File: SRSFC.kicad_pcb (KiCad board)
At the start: 2 copper layers, 6.5 x 0.7 mm, 46 parts, among them J1 SWD_interface, X1 25MHz

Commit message: added BMP388
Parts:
- added CARD1: ~, SD_CARD_READER:TF-SMD_TF-PUSH, F.Cu at (166.5, 99.1)
- moved H4 40.4 mm to (167.9, 112.8)
- moved USB1 34.9 mm to (114.3, 98.7)
- moved X1 28.9 mm to (128.9, 97.9)
- moved SW1 20.1 mm to (148.2, 100.6)
- moved U4 12.5 mm to (147.8, 105.4)
- moved H3 4.83 mm to (120.4, 112.8)
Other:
- board size 6.5 x 0.7 mm -> 1.2 x 9.2 mm

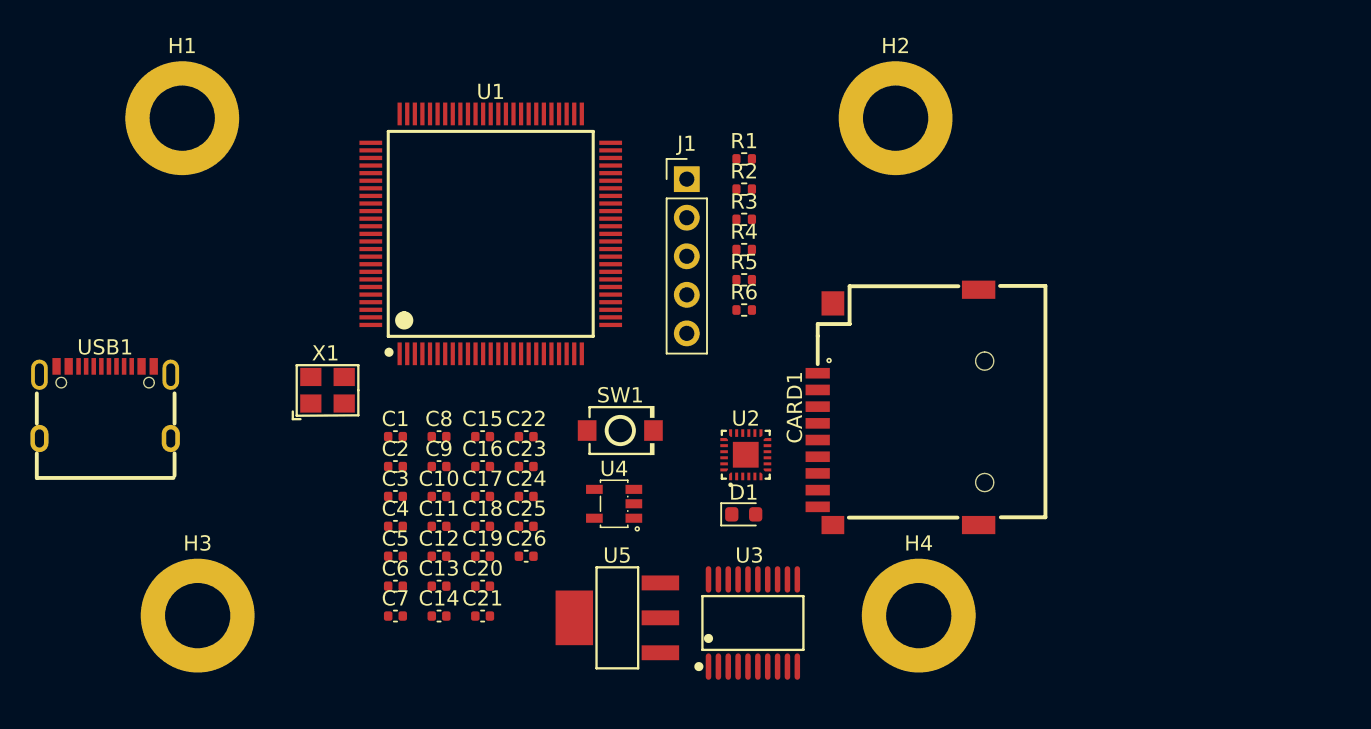
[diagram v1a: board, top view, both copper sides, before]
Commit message: added servo connectors, schema done (probably)
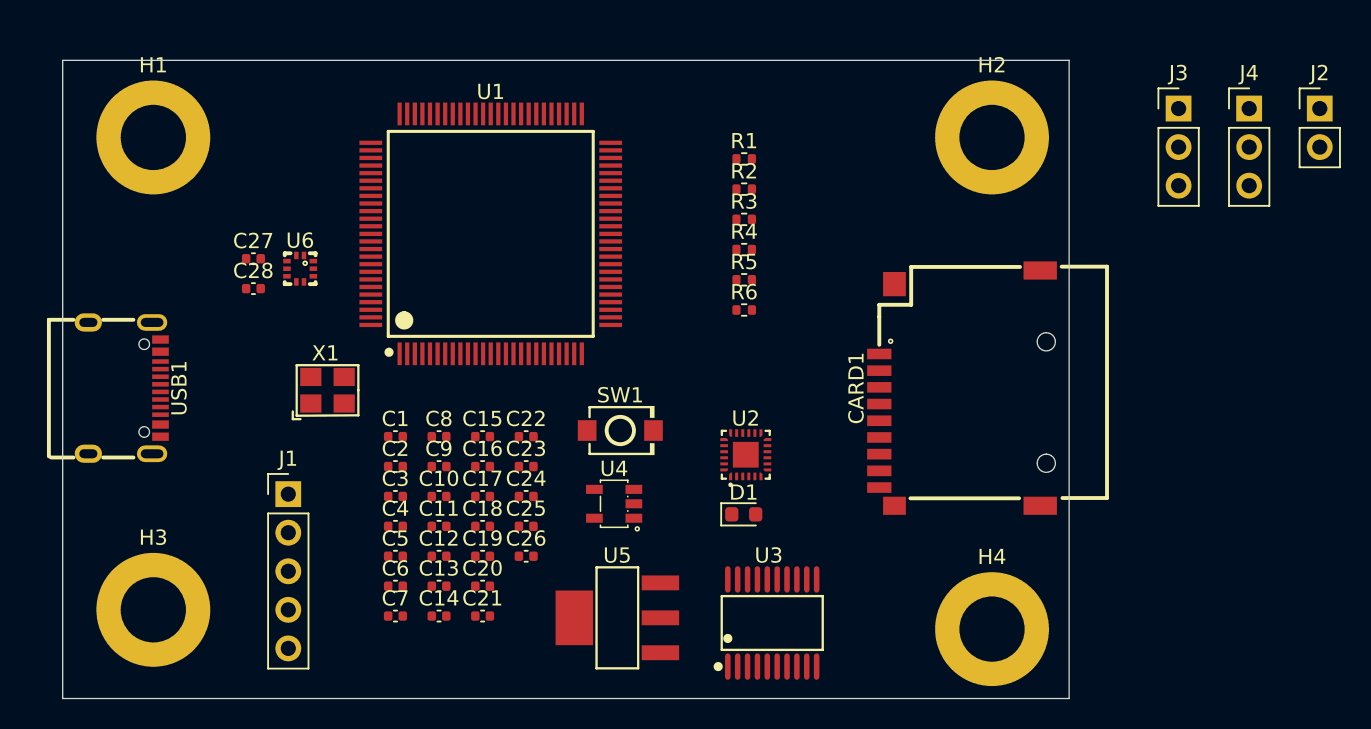
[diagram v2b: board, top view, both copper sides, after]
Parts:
- added C27: .1uF, Capacitor_SMD:C_0402_1005Metric, F.Cu at (124.1, 89.3)
- added C28: 100nF, Capacitor_SMD:C_0402_1005Metric, F.Cu at (124.1, 91.2)
- added J2: POWER, Connector_PinHeader_2.54mm:PinHeader_1x02_P2.54mm_Vertical, F.Cu at (194.3, 79.4)
- added J3: SERVO1, Connector_PinHeader_2.54mm:PinHeader_1x03_P2.54mm_Vertical, F.Cu at (185.0, 79.4)
- added J4: SERVO2, Connector_PinHeader_2.54mm:PinHeader_1x03_P2.54mm_Vertical, F.Cu at (189.7, 79.4)
- added U6: ~, BMP388:SENSORM-SMD_BMP388, F.Cu at (127.1, 89.9)
- moved J1 33.5 mm to (126.4, 104.8)
- moved H2 6.48 mm to (172.7, 81.3)
- moved H4 4.91 mm to (172.7, 113.7)
- moved CARD1 4.25 mm to (170.6, 97.8)
- moved H3 2.95 mm to (117.5, 112.4)
- moved H1 2.29 mm to (117.5, 81.3)
- moved USB1 1.58 mm to (115.6, 97.8), turned to -90 degrees
- moved U3 1.27 mm to (158.2, 113.3)
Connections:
- net +5V renamed VCC
- CARD1 pad 2: unconnected-(CARD1-CD/DAT3-Pad2) -> /SDIO_D2
- CARD1 pad 3: unconnected-(CARD1-CMD-Pad3) -> /SDIO_D3
- CARD1 pad 4: unconnected-(CARD1-VDD-Pad4) -> +3.3V
- CARD1 pad 5: unconnected-(CARD1-CLX-Pad5) -> /SDIO_SCK
- CARD1 pad 6: unconnected-(CARD1-VSS-Pad6) -> /SDIO_CMD
- CARD1 pad 7: unconnected-(CARD1-DAT0-Pad7) -> /SDIO_D0
- CARD1 pad 8: unconnected-(CARD1-DAT1-Pad8) -> /SDIO_D1
- CARD1 pad CD: unconnected-(CARD1-PadCD) -> GND
- U1 pad 65: unconnected-(U1-PC8-Pad65) -> /SDIO_D0
- U1 pad 66: unconnected-(U1-PC9-Pad66) -> /SDIO_D1
- U1 pad 67: unconnected-(U1-PA8-Pad67) -> /servo_2
- U1 pad 78: unconnected-(U1-PC10-Pad78) -> /SDIO_D2
- U1 pad 79: unconnected-(U1-PC11-Pad79) -> /SDIO_D3
- U1 pad 80: unconnected-(U1-PC12-Pad80) -> /SDIO_SCK
- U1 pad 83: unconnected-(U1-PD2-Pad83) -> /SDIO_CMD
- U1 pad 92: unconnected-(U1-PB6-Pad92) -> /servo_1
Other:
- board size 1.2 x 9.2 mm -> 66.3 x 42 mm
- copper layers 2 -> 4

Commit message: finished v1 (bad) layout)
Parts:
- C27: value .1uF -> 100nF
- R2: value 1k -> 220
- moved J2 57.7 mm to (147.3, 112.8), turned to 90 degrees
- moved J3 57.3 mm to (138.4, 112.8), turned to 90 degrees
- moved J4 53.6 mm to (144.8, 108.7), turned to 90 degrees
- moved D1 47.0 mm to (113.3, 87.4), turned to 90 degrees
- moved R2 41.4 mm to (115.1, 87.4), turned to -90 degrees
- moved R3 40.1 mm to (119.9, 103.4)
- moved R1 39.7 mm to (125.7, 108.0), turned to 90 degrees
- moved R4 38.2 mm to (119.9, 100.1)
- moved U5 37.7 mm to (116.3, 92.5)
- moved R5 35.7 mm to (126.5, 110.2), turned to 180 degrees
- moved R6 32.7 mm to (128.8, 110.2)
- moved C27 32.2 mm to (154.4, 100.1), turned to 90 degrees
- moved C25 28.6 mm to (119.9, 88.8)
- moved C24 28.1 mm to (119.9, 87.6)
- moved SW1 25.8 mm to (123.4, 107.7), turned to 90 degrees
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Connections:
- U1 pad 93: unconnected-(U1-PB7-Pad93) -> /bmp_sda
- U1 pad 95: unconnected-(U1-PB8-Pad95) -> /bmp_scl
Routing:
- net VCC: track 0.00 -> 67.2 mm
- net GND: track 0.00 -> 60.5 mm, vias 0 -> 30
- net +3.3V: track 0.00 -> 59.5 mm, vias 0 -> 16
- net /SDIO_D0: track 0.00 -> 35.8 mm, vias 0 -> 2
- net /boot0: track 0.00 -> 35.2 mm, vias 0 -> 1
- net /SDIO_D1: track 0.00 -> 35.0 mm
- net /SDIO_CMD: track 0.00 -> 35.0 mm, vias 0 -> 2
- net /SDIO_D2: track 0.00 -> 32.7 mm, vias 0 -> 2
- net /SDIO_SCK: track 0.00 -> 31.9 mm, vias 0 -> 2
- net /SDIO_D3: track 0.00 -> 31.4 mm, vias 0 -> 2
- net +1V8: track 0.00 -> 29.6 mm, vias 0 -> 3
- net /SWCLK: track 0.00 -> 27.1 mm, vias 0 -> 3
- net /USB+: track 0.00 -> 23.5 mm, vias 0 -> 2
- net /servo_1: track 0.00 -> 23.5 mm, vias 0 -> 1
- net /USB-: track 0.00 -> 22.8 mm, vias 0 -> 2
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- added copper zone on In1.Cu, net +3.3V
- added copper zone on In2.Cu, net GND
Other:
- board size 66.3 x 42 mm -> 59.9 x 37.7 mm

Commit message: good layout done, DRC passes
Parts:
- moved USB1 44.4 mm to (157.0, 85.4), turned to 180 degrees
- moved R4 36.5 mm to (155.2, 90.7), turned to -90 degrees
- moved R3 36.3 mm to (153.9, 90.7), turned to -90 degrees
- moved U5 32.2 mm to (148.1, 87.1), turned to -90 degrees
- moved C25 31.5 mm to (151.1, 92.5), turned to -90 degrees
- moved C24 30.4 mm to (149.9, 92.5), turned to -90 degrees
- moved D1 27.3 mm to (140.5, 84.3)
- moved C23 27.2 mm to (148.6, 92.5)
- moved R2 27.1 mm to (142.0, 84.3)
- moved C22 25.9 mm to (147.3, 92.5), turned to -90 degrees
- moved C1 14.2 mm to (139.4, 89.2), turned to 180 degrees
- moved C26 10.2 mm to (141.3, 110.2)
- moved J4 10.2 mm to (155.0, 109.0)
- moved J1 10.2 mm to (134.6, 112.8)
- moved J2 10.2 mm to (157.5, 112.8)
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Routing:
- net /USB-: track 22.8 -> 41.5 mm
- net /USB+: track 23.5 -> 38.9 mm
- net /SWCLK: track 27.1 -> 15.6 mm, vias 3 -> 4
- net /boot0: track 35.2 -> 46.5 mm
- net /servo_2: track 20.3 -> 30.1 mm
- net /servo_1: track 23.5 -> 32.0 mm
- net VCC: track 67.2 -> 59.3 mm
- net /SWDIO: track 17.2 -> 21.1 mm
- net Net-(USB1-CC1): track 1.47 -> 5.12 mm
- net Net-(USB1-CC2): track 1.37 -> 2.91 mm
- net GND: track 60.5 -> 61.6 mm, vias 30 -> 29
- net /nrst: track 8.76 -> 9.93 mm, vias 2 -> 0
- net +3.3V: track 59.5 -> 58.4 mm, vias 16 -> 18
- net /SDIO_CMD: track 35.0 -> 34.1 mm
- net /SDIO_D0: track 35.8 -> 35.2 mm
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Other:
- board size 59.9 x 37.7 mm -> 52.6 x 33.8 mm

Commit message: updated readme
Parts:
- removed C17, C18, C20: 100nF, Capacitor_SMD:C_0402_1005Metric
- removed C19, C21: 1uF, Capacitor_SMD:C_0402_1005Metric
- removed U3: ~, TXS0108EPWR:TSSOP-20_L6.5-W4.4-P0.65-LS6.4-BL
- removed U4: ~, LP5907MFX-1.8:SOT-23-5_L3.0-W1.7-P0.95-LS2.8-BR
- added J5: SERVO3, Connector_PinHeader_2.54mm:PinHeader_1x03_P2.54mm_Vertical, F.Cu at (147.1, 104.9)
- added J6: SERVO4, Connector_PinHeader_2.54mm:PinHeader_1x03_P2.54mm_Vertical, F.Cu at (147.1, 101.1)
- added J7: SERVO5, Connector_PinHeader_2.54mm:PinHeader_1x03_P2.54mm_Vertical, F.Cu at (147.1, 97.3)
- added JP1: address_select, Jumper:SolderJumper-2_P1.3mm_Open_RoundedPad1.0x1.5mm, B.Cu at (147.2, 109.5)
- added JP2: address_select, Jumper:SolderJumper-2_P1.3mm_Open_RoundedPad1.0x1.5mm, B.Cu at (150.7, 109.5)
- added R10: 4.7k, Resistor_SMD:R_0402_1005Metric, F.Cu at (143.5, 90.4)
- added R7: 10k, Resistor_SMD:R_0402_1005Metric, F.Cu at (143.8, 97.5)
- added R8: 10k, Resistor_SMD:R_0402_1005Metric, F.Cu at (143.8, 109.5)
- added R9: 4.7k, Resistor_SMD:R_0402_1005Metric, F.Cu at (143.5, 89.2)
- C15: value 1uF -> 100nF
- U2: footprint ICM-20948:QFN-24_L3.0-W3.0-P0.40-BL-EP -> LSM6DSOWTR:LGA-14L_L3.0-W2.5-P0.50-TL
- moved C16 11.7 mm to (143.8, 103.9), turned to 180 degrees
- moved C15 10.3 mm to (143.7, 98.8), turned to 180 degrees
- moved U2 7.72 mm to (143.8, 101.3), turned to 90 degrees
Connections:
- C15 pad 2: +1V8 -> +3.3V
- C16 pad 1: GND -> +3.3V
- C16 pad 2: +1V8 -> GND
- U1 pad 63: unconnected-(U1-PC6-Pad63) -> /servo_3
- U1 pad 64: unconnected-(U1-PC7-Pad64) -> /servo_4
- U1 pad 68: unconnected-(U1-PA9-Pad68) -> /servo_5
- U1 pad 77: /SPI_CS -> unconnected-(U1-PA15-Pad77)
- U1 pad 88: /SPI_MOSI -> unconnected-(U1-PD7-Pad88)
- U1 pad 89: /SPI_SCK -> unconnected-(U1-PB3-Pad89)
- U1 pad 90: /SPI_MISO -> unconnected-(U1-PB4-Pad90)
- U2 pad 1: unconnected-(U2-NC-Pad1) -> Net-(JP1-A)
- U2 pad 10: Net-(U2-REGOUT) -> unconnected-(U2-OCS_Aux-Pad10)
- U2 pad 12: unconnected-(U2-INT1-Pad12) -> Net-(U2-CS)
- U2 pad 13: +1V8 -> /bmp_scl
- U2 pad 14: unconnected-(U2-NC-Pad14) -> /bmp_sda
- U2 pad 2: unconnected-(U2-NC-Pad2) -> GND
- U2 pad 3: unconnected-(U2-NC-Pad3) -> GND
- U2 pad 5: unconnected-(U2-NC-Pad5) -> +3.3V
- U2 pad 6: unconnected-(U2-NC-Pad6) -> GND
- U2 pad 7: unconnected-(U2-AUX_CL-Pad7) -> GND
- U2 pad 8: +1V8 -> +3.3V
- U2 pad 9: /MISO -> unconnected-(U2-INT2-Pad9)
- U6 pad 5: unconnected-(U6-SDO-Pad5) -> Net-(JP2-A)
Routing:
- net Net-(JP1-A): track 0.00 -> 51.7 mm, vias 0 -> 3
- net Net-(JP2-A): track 0.00 -> 50.5 mm, vias 0 -> 1
- net /servo_3: track 0.00 -> 34.6 mm, vias 0 -> 1
- net /servo_4: track 0.00 -> 30.6 mm, vias 0 -> 1
- net +1V8: track 29.6 -> 0.00 mm, vias 2 -> 0
- net /servo_5: track 0.00 -> 29.1 mm, vias 0 -> 3
- net VCC: track 59.3 -> 77.3 mm, vias 0 -> 1
- net /bmp_sda: track 3.88 -> 19.6 mm, vias 0 -> 2
- net /SPI_MOSI: track 13.1 -> 0.00 mm, vias 2 -> 0
- net /SPI_MISO: track 12.5 -> 0.00 mm, vias 2 -> 0
- net /SPI_CS: track 11.5 -> 0.00 mm
- net /SPI_SCK: track 10.5 -> 0.00 mm, vias 2 -> 0
- net /bmp_scl: track 5.12 -> 15.6 mm, vias 2 -> 3
- net /MISO: track 10.3 -> 0.00 mm, vias 2 -> 0
- net Net-(U2-CS): track 0.00 -> 6.28 mm
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
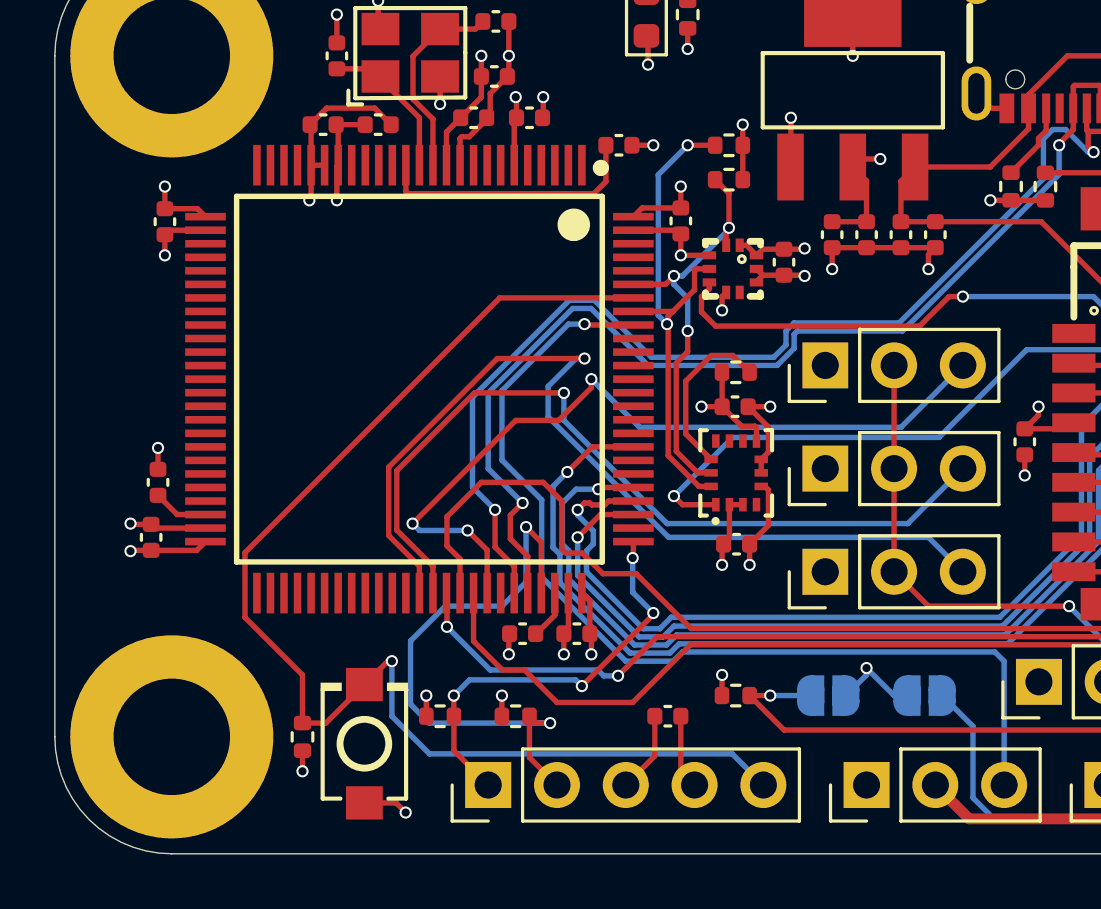
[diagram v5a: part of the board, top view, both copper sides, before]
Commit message: added silkscreen, added UART interface
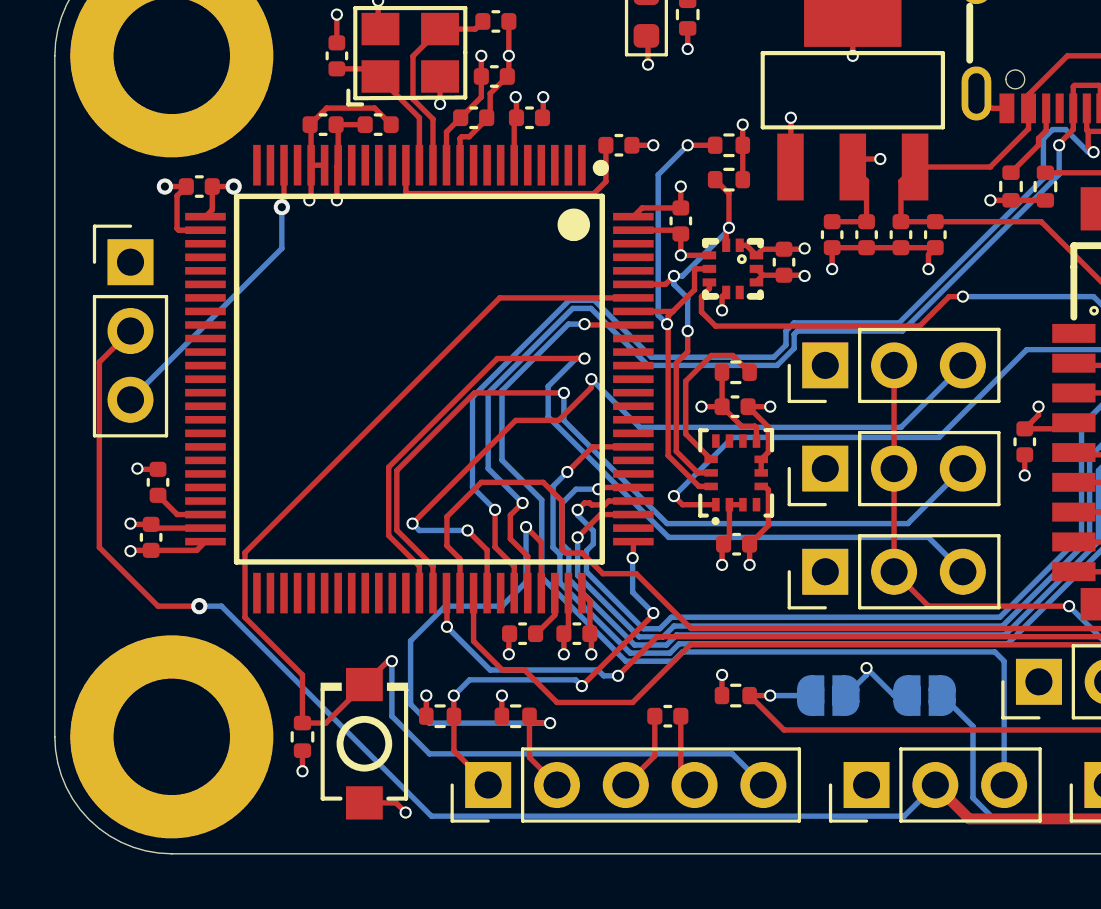
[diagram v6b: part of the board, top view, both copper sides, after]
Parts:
- added J8: IBUS_RX, Connector_PinHeader_2.54mm:PinHeader_1x03_P2.54mm_Vertical, F.Cu at (121.4, 93.5)
- moved C8 1.82 mm to (124.0, 90.7), turned to 0 degrees
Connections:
- U1 pad 23: unconnected-(U1-PA1-Pad23) -> /IBUS_RX
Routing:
- net VCC: track 77.3 -> 121.2 mm, vias 1 -> 2
- net /IBUS_RX: track 0.00 -> 11.0 mm, vias 0 -> 1
- net +3.3V: track 53.5 -> 54.8 mm
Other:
- board text added: "Designed by avaninder.com"
- board text added: "FC V1.0"
- board text added: "SRS"
